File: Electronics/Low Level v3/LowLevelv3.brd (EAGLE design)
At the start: 117.3 x 74.9 mm, 53 parts, among them IC2 MCP4802, K1 ORWH-SH-105D1F,000, K3 ORWH-SH-105D1F,000, Q1 16MHz, T1 2N3904, T2 2N3904, U1 284512-4, U4 MCP2515, U5 MCP2551DIL08, X1 DB9 Plug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

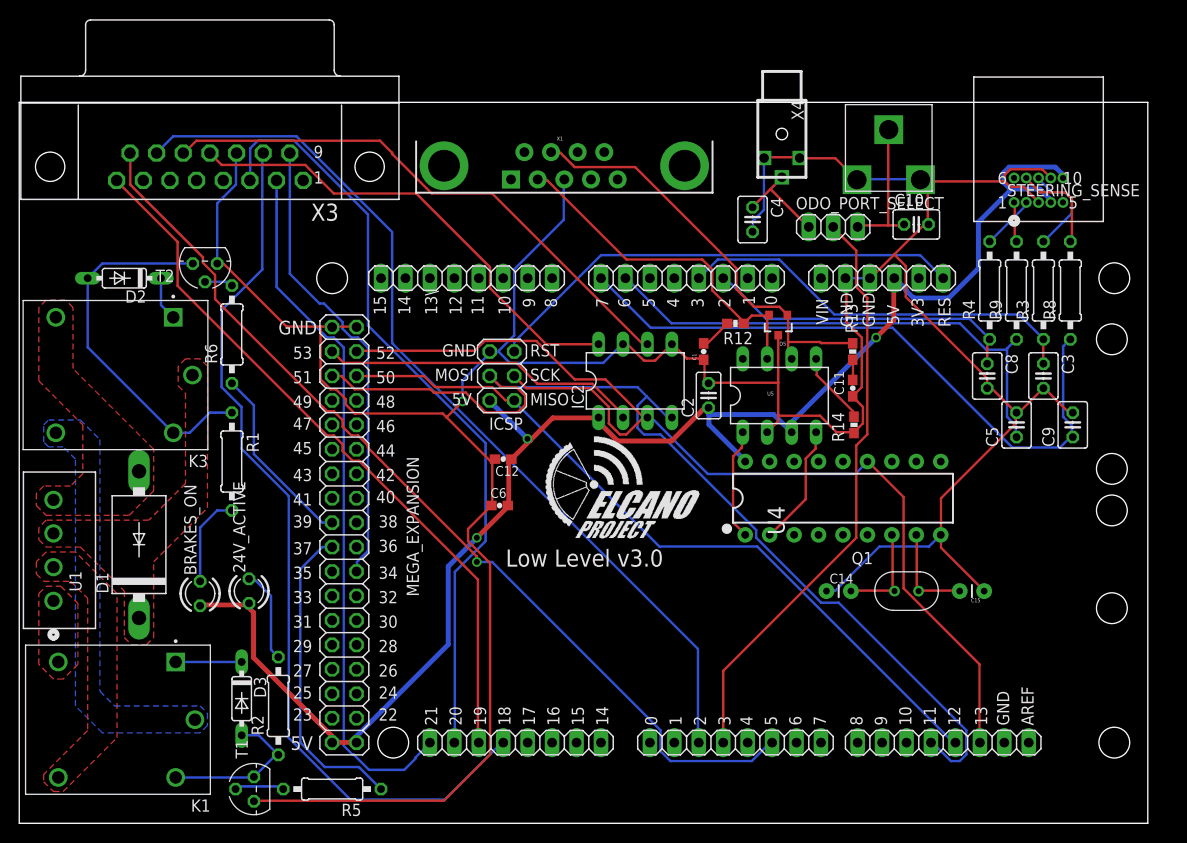
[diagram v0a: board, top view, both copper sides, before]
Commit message: electronics update!
moved a lot of stuff to get the board smaller, added ground planes, added CANbus 3-pin header, fixed all the silkscreening
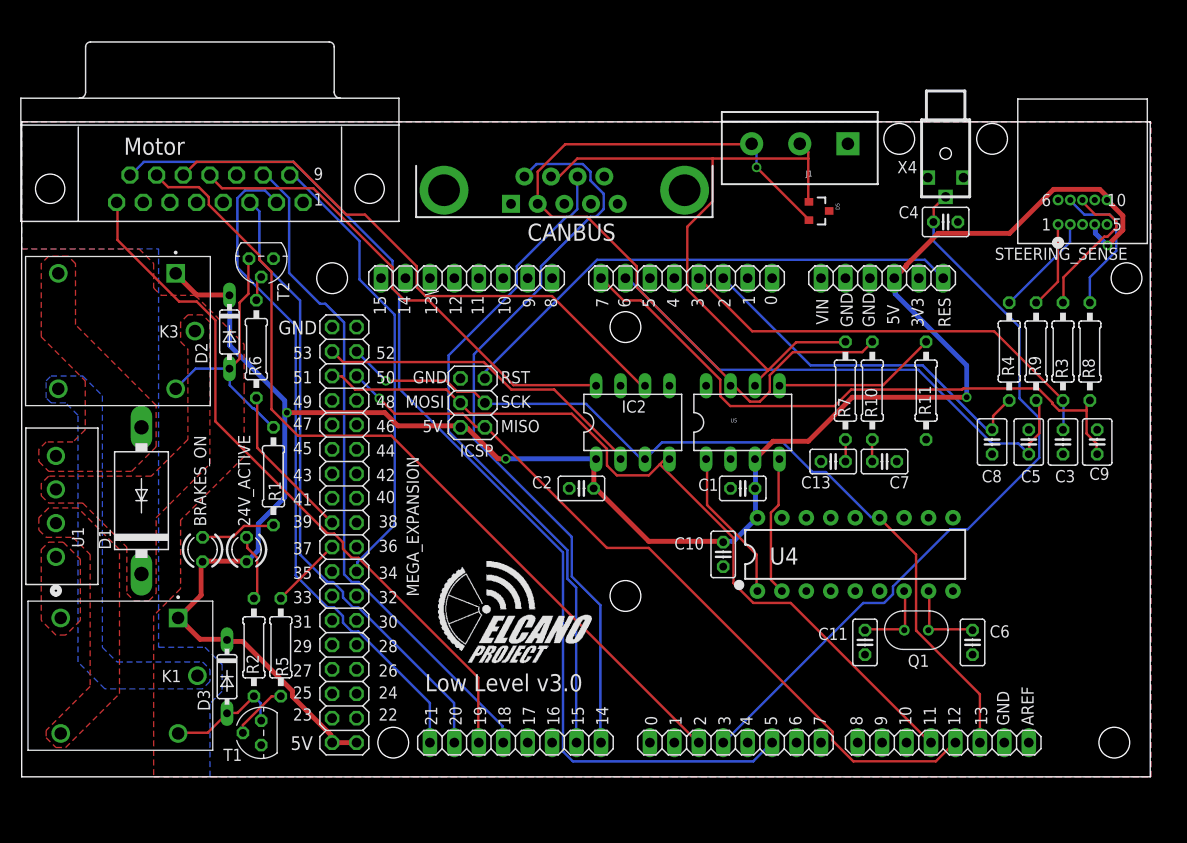
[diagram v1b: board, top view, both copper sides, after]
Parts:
- removed C12: 0.1uF, SparkFun-Capacitors:0603-CAP
- removed C14, C15: 22pF, SparkFun-Capacitors:CAP-PTH-2.54
- removed ODO_PORT_SELECT: (no value), pinhead:1X03
- removed R12, R13: 100, SparkFun-Resistors:0603-RES
- removed R14: 4.7K, SparkFun-Resistors:0603-RES
- removed U$2: CUI_JACKTHROUGH_HOLE, Elcano:CUIJACK
- removed X1: DB9 Plug, SparkFun-Connectors:DB9
- added C13, C7: 560pF, rcl:C025-025X050
- added CANBUS: DB9 Plug, SparkFun-Connectors:DB9
- added J1: (no value), SparkFun-Connectors:SCREWTERMINAL-5MM-3
- added R10, R7: 100, rcl:0207/10
- added R11: 4.7K, rcl:0207/10
- C1: value 560pF -> 0.1uF; device SparkFun-Capacitors:0603-CAP -> rcl:C025-025X050
- C10: value 1 uF -> 0.1uF; device rcl:C025-030X050 -> rcl:C025-025X050
- C11: value 560pF -> 22pF; device SparkFun-Capacitors:0603-CAP -> rcl:C025-025X050
- C6: value 0.1uF -> 22pF; device SparkFun-Capacitors:0603-CAP -> rcl:C025-025X050
- moved C6 51.2 mm to (99.8, 19.6), turned to 270 degrees
- moved C10 39.7 mm to (73.9, 28.7), turned to 270 degrees
- moved C11 26.4 mm to (88.6, 19.6), turned to 270 degrees
- moved C4 20.1 mm to (97.0, 63.2), turned to 0 degrees
- moved X4 17.1 mm to (97.0, 70.4)
- moved C2 16.4 mm to (59.2, 35.6), turned to 180 degrees
- moved R5 15.7 mm to (27.9, 19.1), turned to 270 degrees
- moved C1 14.8 mm to (75.9, 35.6), turned to 180 degrees
- moved D5 12.5 mm to (83.8, 64.4), turned to 270 degrees
- moved D2 12.3 mm to (22.6, 51.8), turned to 270 degrees
- moved C3 7.15 mm to (109.2, 40.4)
- moved C8 6.88 mm to (101.9, 40.4)
- moved R4 6.67 mm to (103.6, 49.8)
- moved R3 6.67 mm to (109.2, 49.8)
- moved R8 6.67 mm to (112.0, 49.8)
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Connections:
- net SOLENOID_GND renamed SOLENOID_COMMON
- removed net N$1: C10.1, ODO_PORT_SELECT.3, U$2.P$1
- removed net N$15: D2.C, K3.1
- removed net N$4: C4.1, ODO_PORT_SELECT.1, X4.P$1
- removed net N$8: D3.C, K1.1
- new net RX3: CANBUS.8, COMM_DIG.7
- new net TX3: CANBUS.6, COMM_DIG.8
- net 5V: now also C1.1, C10.1, D2.C, D3.C, K1.1, K3.1; no longer C12.2, C6.2
- net CANH: now also CANBUS.7, J1.2, R7.2; no longer R13.2, X1.7
- net CANL: now also CANBUS.2, J1.3, R10.2; no longer R12.2, X1.2
- net GND: now also C1.2, C11.2, C13.2, C6.2, C7.2, CANBUS.1, CANBUS.3, J1.1, R11.2; no longer C1.1, C11.1, C12.1, C14.1, C15.1, C6.1, R14.1, U$2.P$2, U$2.P$3, X1.3
- net N$10: now also C13.1, R7.1; no longer C11.2, R13.1
- net N$14: now also R11.1; no longer R14.2
- net N$17: now also C6.1; no longer C15.2
- net N$18: now also C11.1; no longer C14.2
- net N$9: now also C7.1, R10.1; no longer C1.2, R12.1
- net WHEELROTATION: now also C4.1, X4.P$1; no longer ODO_PORT_SELECT.2
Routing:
- net GND: track 348.1 -> 0.00 mm, vias 1 -> 0
- net TX3: track 0.00 -> 79.1 mm
- net RX3: track 0.00 -> 70.1 mm
- net 5V: track 164.8 -> 214.4 mm, vias 3 -> 4
- net CANL: track 36.7 -> 85.6 mm, vias 0 -> 1
- net CANH: track 44.4 -> 71.9 mm
- net VOLTAGE_SWITCH: track 32.7 -> 7.58 mm
- net 3MOSI: track 106.8 -> 84.0 mm
- net EBIKECONTRL: track 92.9 -> 70.3 mm
- net SCK: track 112.0 -> 90.7 mm, vias 0 -> 1
- net WHEELROTATION: track 61.3 -> 77.8 mm
- net N$1: track 14.9 -> 0.00 mm
- net HALLPHASEB: track 80.4 -> 65.7 mm
- net WATCHDOG: track 99.6 -> 113.4 mm, vias 1 -> 0
- net N$12: track 38.3 -> 26.9 mm
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- added copper zone on layer 1, net GND
- added copper zone on layer 16, net GND
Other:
- board size 117.3 x 74.9 mm -> 117.3 x 68.1 mm

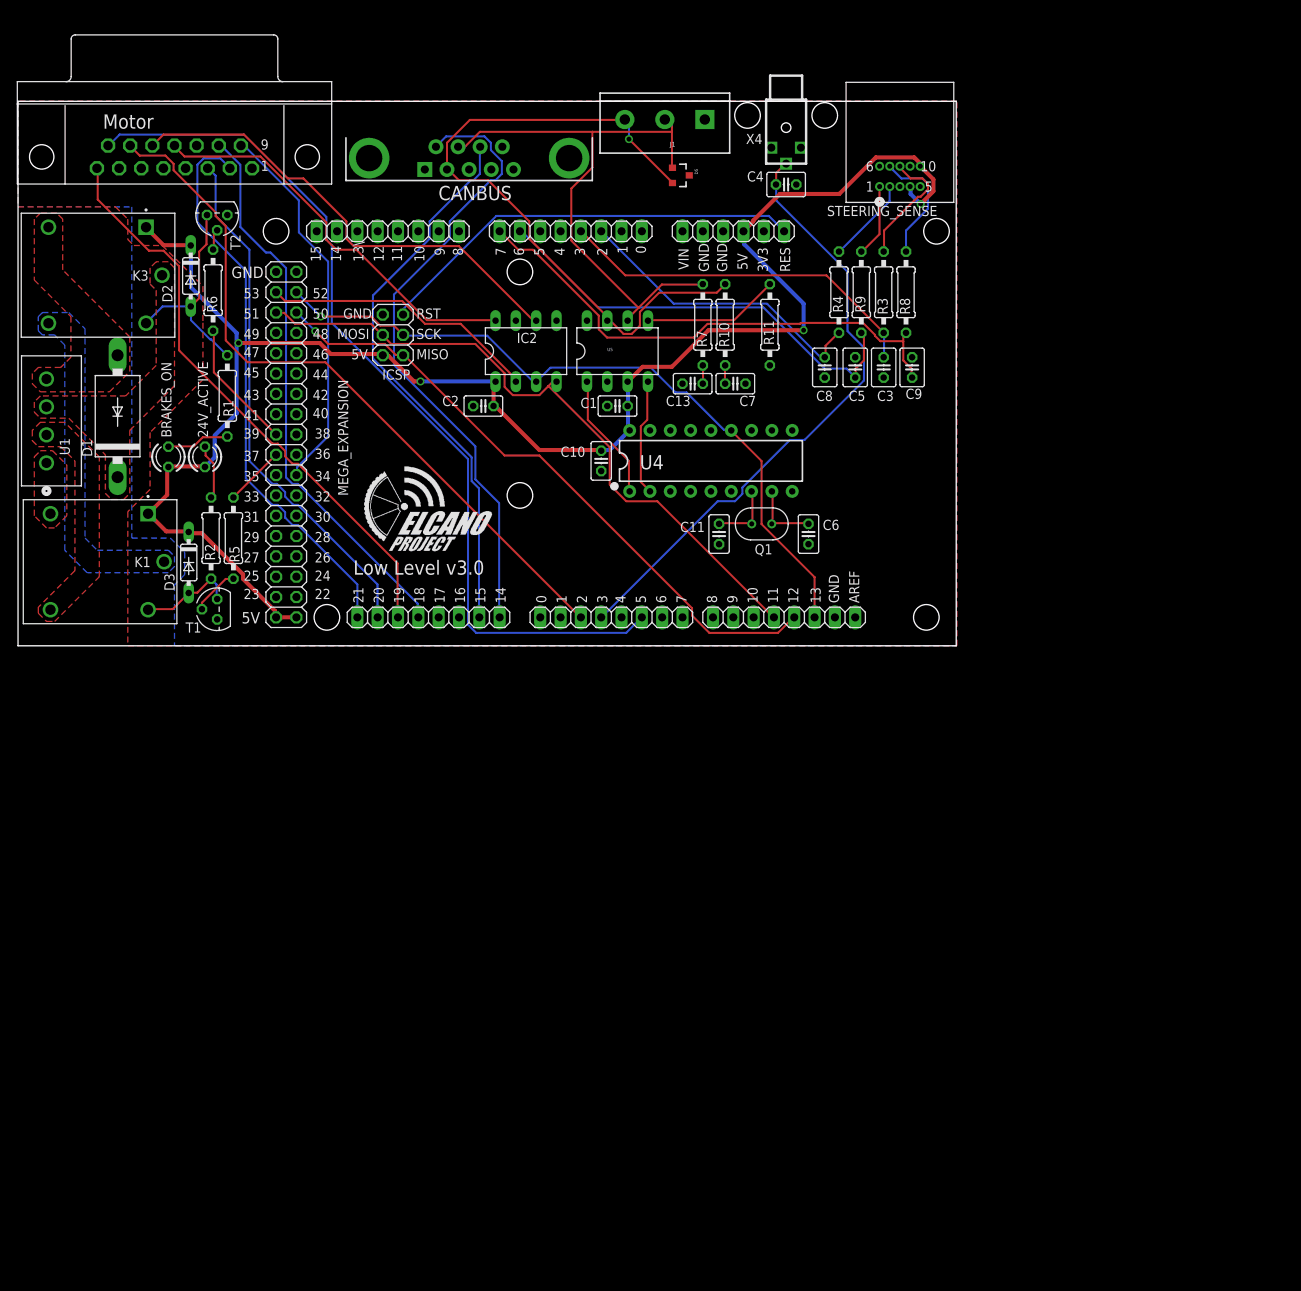
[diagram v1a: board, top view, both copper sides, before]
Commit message: added PWM output on steering header and 120ohm terminating resistor for CAN
forgot to commit this...
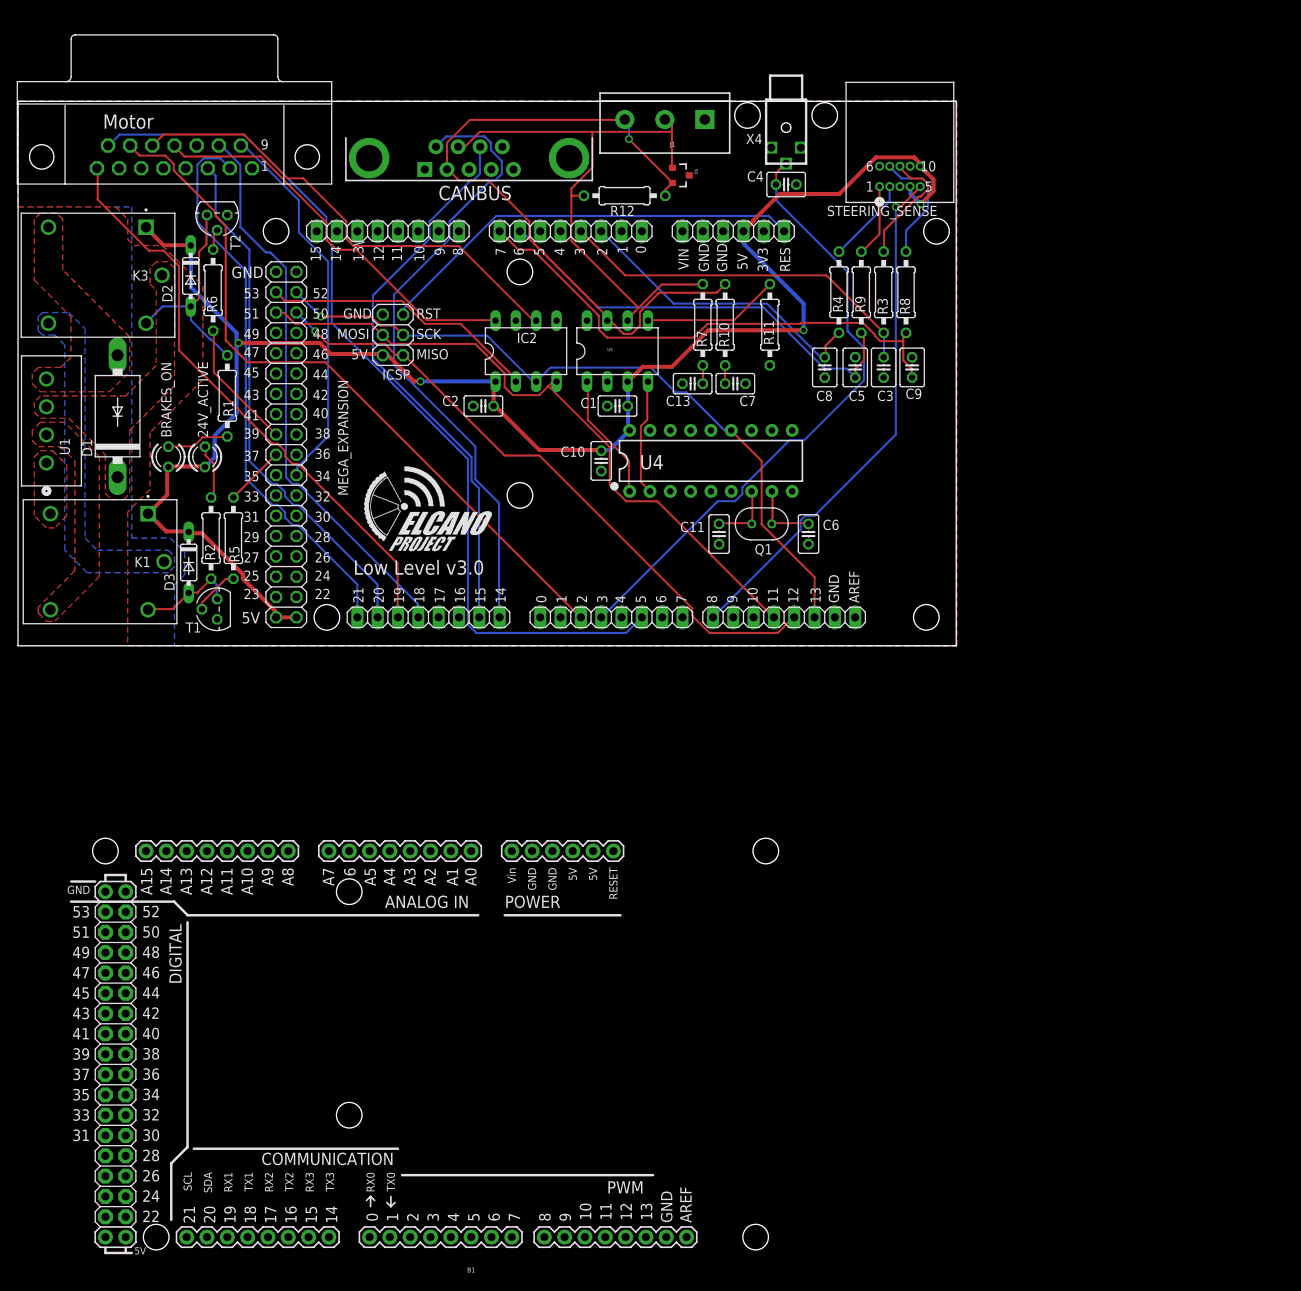
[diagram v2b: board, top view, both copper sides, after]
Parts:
- added B1: ARDUINO_MEGA_R3FULL, SparkFun-Boards:ARDUINO_MEGA
- added R12: 120, rcl:0207/10
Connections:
- new net STEER_SERVO_PWM: D8-13.1, STEERING_SENSE.5
- net CANH: now also R12.2
- net CANL: now also R12.1
- net GND: now also STEERING_SENSE.6
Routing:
- net STEER_SERVO_PWM: track 0.00 -> 65.6 mm, vias 0 -> 1
- net CANL: track 85.6 -> 87.6 mm
- net CANH: track 71.9 -> 73.6 mm
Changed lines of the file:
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@@
 <attribute name="VALUE" x="83.439" y="69.469" size="0.6096" layer="27" font="vector" ratio="20" rot="R180"/>
+</element>
+<element name="R12" library="rcl" library_urn="urn:adsk.eagle:library:334" package="0207/10" package3d_urn="urn:adsk.eagle:package:23491/2" value="120" x="76.835" y="61.849" smashed="yes" rot="R180">
+<attribute name="NAME" x="78.105" y="60.579" size="1.27" layer="25" ratio="10" rot="R180"/>
+<attribute name="SPICEPREFIX" value="R" x="76.835" y="61.849" size="1.778" layer="27" rot="R180" display="off"/>
+<attribute name="VALUE" x="77.3176" y="62.484" size="1.27" layer="27" ratio="10" rot="R180"/>
+</element>
+<element name="B1" library="SparkFun-Boards" library_urn="urn:adsk.eagle:library:509" package="ARDUINO_MEGA" package3d_urn="urn:adsk.eagle:package:37320/1" value="ARDUINO_MEGA_R3FULL" x="58.928" y="-44.196" smashed="yes" rot="R180">
+<attribute name="NAME" x="57.658" y="-72.136" size="0.6096" layer="25" font="vector" ratio="20" rot="R180" align="bottom-center"/>
+<attribute name="VALUE" x="58.928" y="-16.256" size="0.6096" layer="27" font="vector" ratio="20" rot="R180" align="top-center"/>
 </element>
 </elements>
@@
 <vertex x="1.016" y="73.66"/>
 </polygon>
+<contactref element="STEERING_SENSE" pad="6"/>
 <wire x1="27.178" y1="59.436" x2="23.3426" y2="68.1203" width="0" layer="19" extent="1-1"/>
 <wire x1="46.609" y1="46.99" x2="35.814" y2="52.324" width="0" layer="19" extent="1-1"/>
@@
 <wire x1="56.1213" y1="68.0085" x2="56.024" y2="67.968" width="0.254" layer="1"/>
 <wire x1="70.1802" y1="56.2356" x2="78.58125" y2="47.83455" width="0.254" layer="1"/>
-<wire x1="70.1802" y1="62.7507" x2="70.1802" y2="56.2356" width="0.254" layer="1"/>
+<wire x1="70.1802" y1="62.7507" x2="70.1802" y2="61.722" width="0.254" layer="1"/>
+<wire x1="70.1802" y1="61.722" x2="70.1802" y2="56.2356" width="0.254" layer="1"/>
 <wire x1="72.8091" y1="65.3796" x2="70.1802" y2="62.7507" width="0.254" layer="1"/>
 <wire x1="72.8091" y1="69.8373" x2="72.8091" y2="65.3796" width="0.254" layer="1"/>
+<contactref element="R12" pad="2"/>
+<wire x1="71.755" y1="61.849" x2="70.3072" y2="61.849" width="0.254" layer="1"/>
+<wire x1="70.3072" y1="61.849" x2="70.1802" y2="61.722" width="0.254" layer="1"/>
 </signal>
 <signal name="CANL">
@@
 <wire x1="54.7497" y1="65.151" x2="54.634" y2="65.128" width="0.254" layer="1"/>
 <via x="77.3811" y="68.9229" extent="1-16" drill="0.6096"/>
+<contactref element="R12" pad="1"/>
+<wire x1="81.915" y1="61.849" x2="81.915" y2="62.534" width="0.254" layer="1"/>
+<wire x1="81.915" y1="62.534" x2="82.82" y2="63.439" width="0.254" layer="1"/>
 </signal>
 <signal name="3.3V" class="1">
@@
 <wire x1="58.7502" y1="67.8942" x2="58.784" y2="67.968" width="0.254" layer="16"/>
 </signal>
+<signal name="STEER_SERVO_PWM">
+<contactref element="D8-13" pad="1"/>
+<contactref element="STEERING_SENSE" pad="5"/>
+<wire x1="110.744" y1="32.004" x2="110.744" y2="60.452" width="0.254" layer="16"/>
+<wire x1="98.8314" y1="21.238325" x2="99.411675" y2="21.8186" width="0.254" layer="16"/>
+<wire x1="87.884" y1="9.144" x2="98.8314" y2="20.0914" width="0.254" layer="16"/>
+<wire x1="100.5586" y1="21.8186" x2="110.744" y2="32.004" width="0.254" layer="16"/>
+<wire x1="98.8314" y1="20.0914" x2="98.8314" y2="21.238325" width="0.254" layer="16"/>
+<wire x1="99.411675" y1="21.8186" x2="100.5586" y2="21.8186" width="0.254" layer="16"/>
+<via x="110.744" y="60.452" extent="1-16" drill="0.6096"/>
+<wire x1="113.4745" y1="62.59745625" x2="113.4745" y2="62.6745" width="0.254" layer="1"/>
+<wire x1="113.4745" y1="62.6745" x2="113.792" y2="62.992" width="0.254" layer="1"/>
+<wire x1="110.744" y1="60.452" x2="111.32904375" y2="60.452" width="0.254" layer="1"/>
+<wire x1="111.32904375" y1="60.452" x2="113.4745" y2="62.59745625" width="0.254" layer="1"/>
+</signal>
 </signals>
